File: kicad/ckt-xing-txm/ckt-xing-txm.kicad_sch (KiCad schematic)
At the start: 33 parts, among them J4 SM04B-SRSS, J5 SM04B-SRSS, U2 ATtiny861A-S, U3 AP7381-33Y

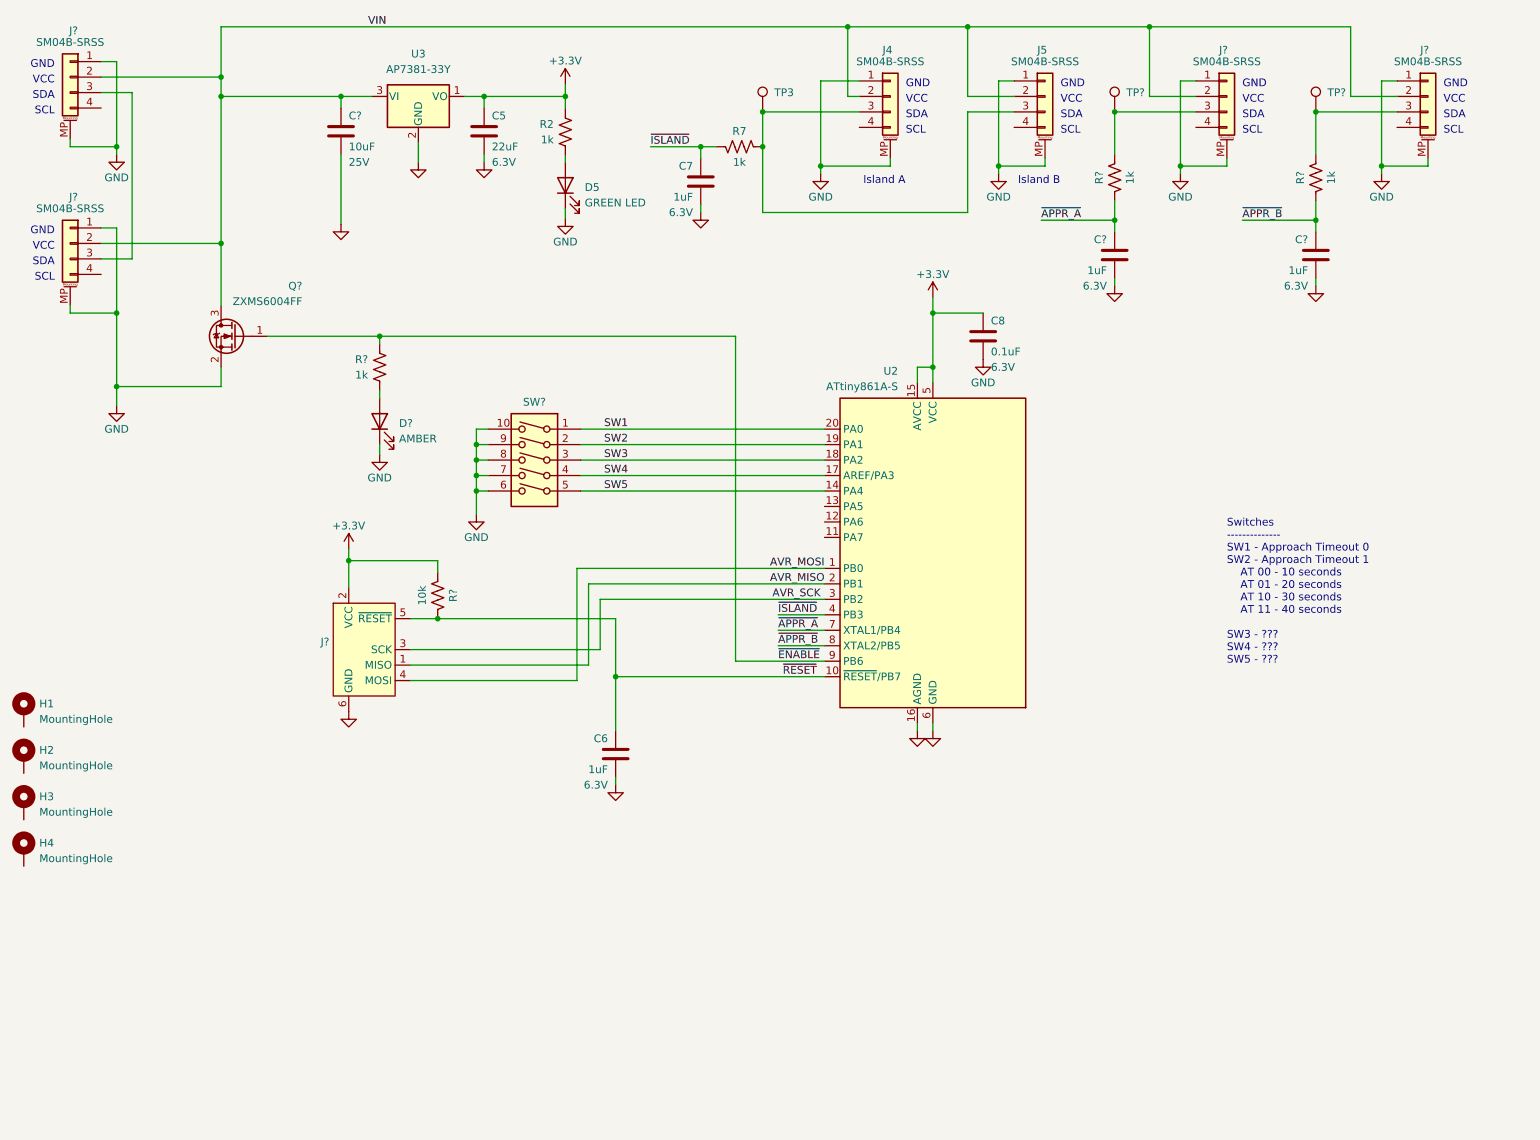
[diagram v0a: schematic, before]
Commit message: Add second track inputs to txm
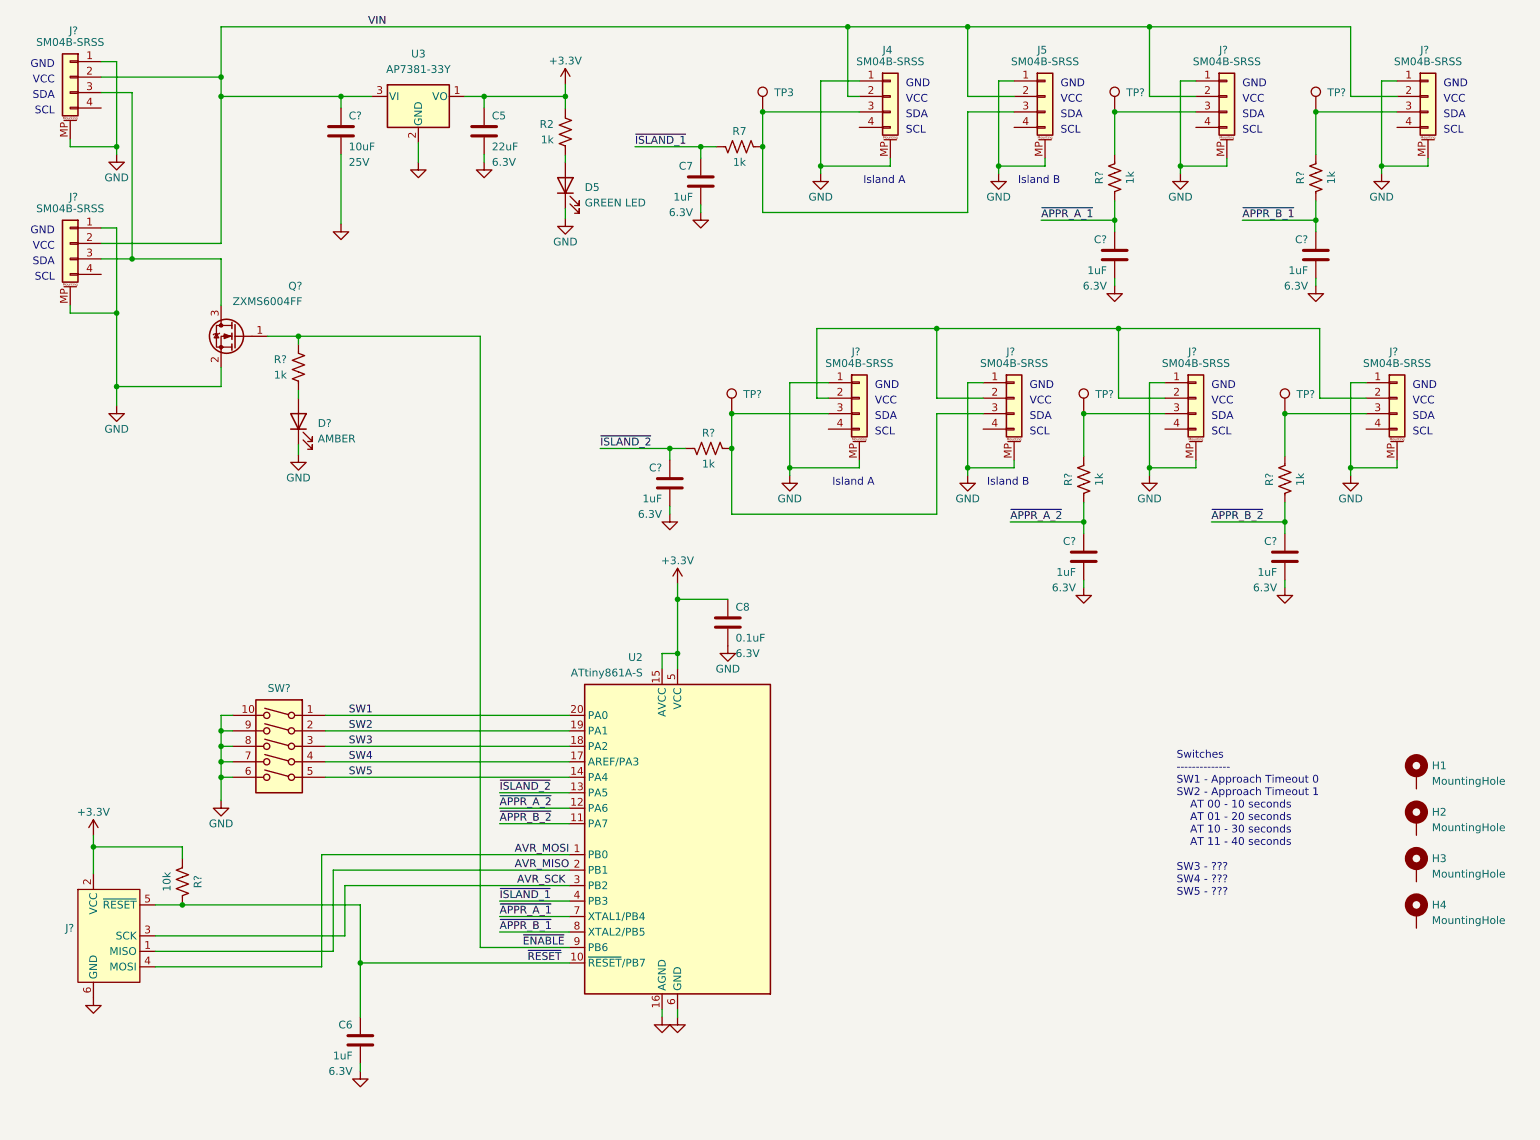
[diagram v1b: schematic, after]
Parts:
- added C? (x3): 1uF, Capacitor_SMD:C_0805_2012Metric, symbol Device:C
- added J? (x4): SM04B-SRSS, Connector_JST:JST_SH_SM04B-SRSS-TB_1x04-1MP_P1.00mm_Horizontal, symbol Connector_Generic_MountingPin:Conn_01x04_MountingPin
- added R? (x3): 1k, Resistor_SMD:R_0805_2012Metric, symbol Device:R_US
- added TP? (x3): TestPoint, TestPoint:TestPoint_Pad_D2.0mm, symbol Connector:TestPoint
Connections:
- net GND: now also C?.2, C?.2, C?.2, J?.1 (Pin_1), J?.1 (Pin_1), J?.1 (Pin_1), J?.1 (Pin_1), J?.MP (MountPin), J?.MP (MountPin), J?.MP (MountPin), J?.MP (MountPin)
- net VIN: no longer Q?.3 (D)
- net ~{APPR_B_2}: now reaches U2.11 (PA7)
- net ~{APPR_B_2}: now also C?.1, R?.2
- net ~{APPR_A_2}: now reaches U2.12 (PA6)
- net ~{APPR_A_2}: now also C?.1, R?.2
- net ~{ISLAND_2}: now reaches U2.13 (PA5)
- net ~{ISLAND_2}: now also C?.1, R?.2
- net at J?.3 (Pin_3), J?.3 (Pin_3): now also Q?.3 (D)
- net ~{APPR_A} renamed ~{APPR_A_1}
- net ~{APPR_B} renamed ~{APPR_B_1}
- net ~{ISLAND} renamed ~{ISLAND_1}
- new net: J?.3 (Pin_3), R?.1, TP?.1 (x2)
- new net: J?.2 (Pin_2), J?.2 (Pin_2), J?.2 (Pin_2), J?.2 (Pin_2)
- new net: J?.3 (Pin_3), J?.3 (Pin_3), R?.1, TP?.1
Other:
- moved on the sheet: C6, C8, D?, H1, H2, H3, H4, J?, R?, SW?, U2

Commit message: Initial layout of TXM board
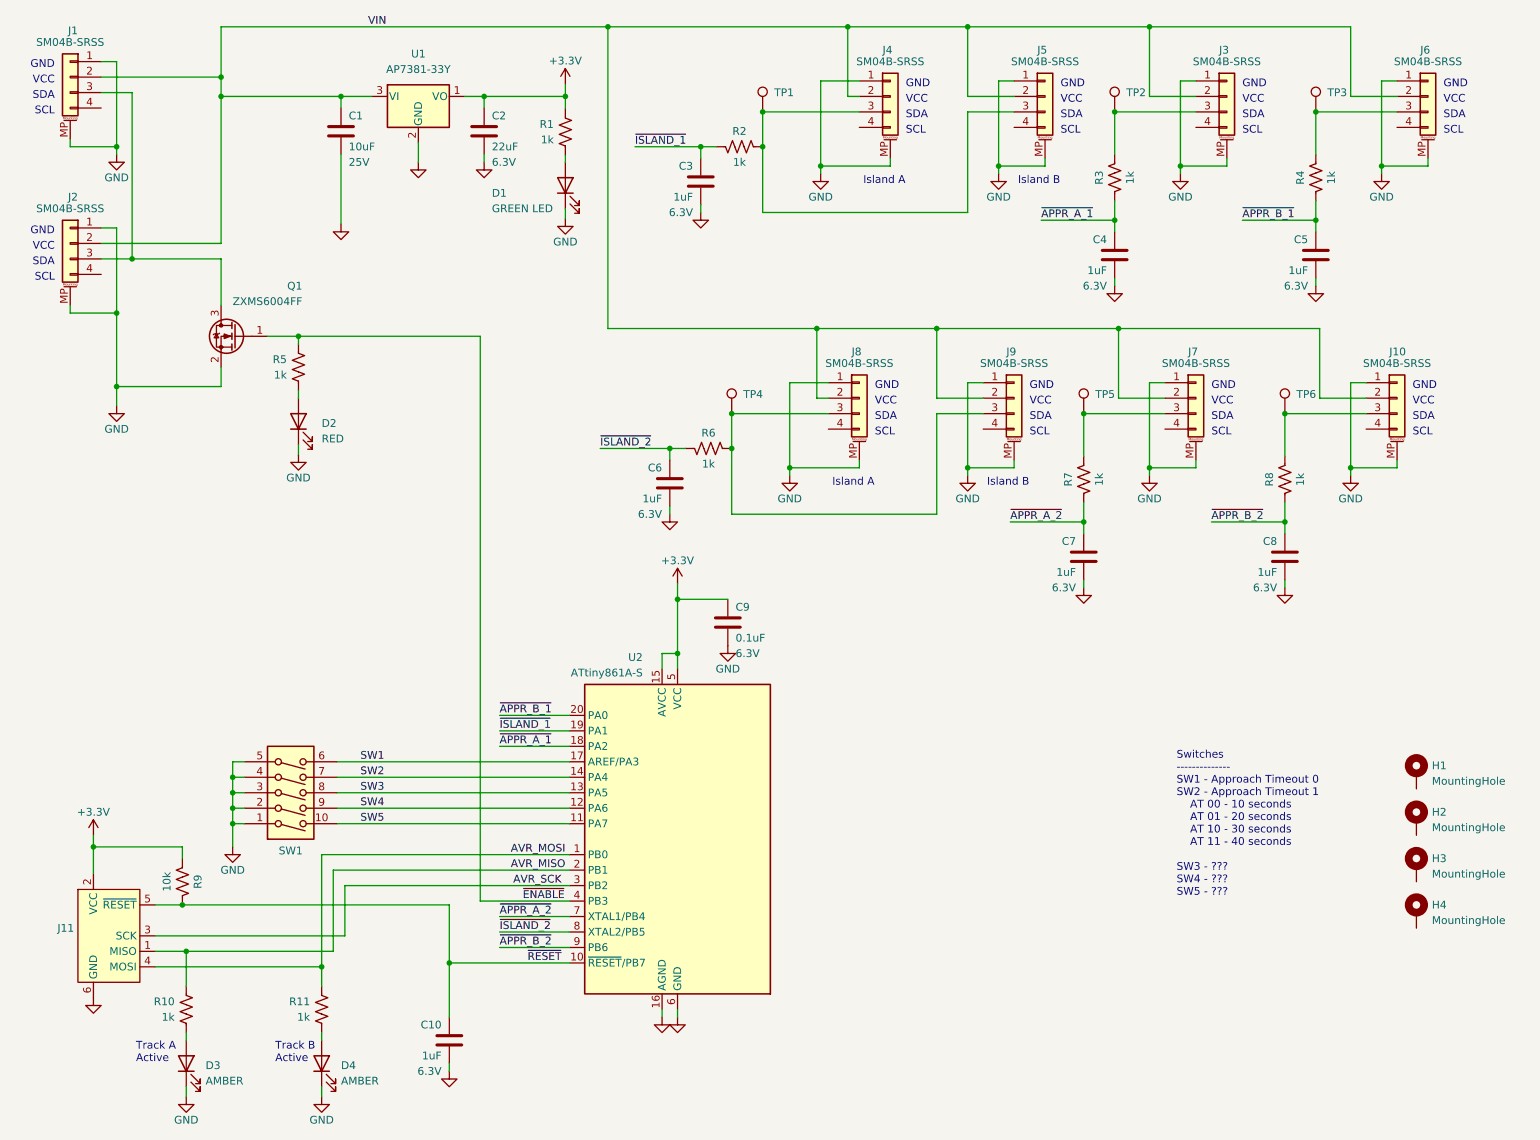
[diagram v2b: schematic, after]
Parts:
- removed SW?: SW_DIP_x05, ISE_UltraLibrarian:CST_219SMT, symbol Switch:SW_DIP_x05
- added D3, D4: AMBER, LED_SMD:LED_0805_2012Metric, symbol Device:LED
- added R10, R11: 1k, Resistor_SMD:R_0805_2012Metric, symbol Device:R_US
- added SW1: SW_DIP_x05, ISE_UltraLibrarian:CST_219SMT, symbol Switch:SW_DIP_x05
- D2: renamed from D?; value AMBER -> RED
- gave numbers to parts that had none: 28
- renumbered C6 to C10, C5 to C2, C7 to C3, C8 to C9, D5 to D1, R2 to R1, R7 to R2, TP3 to TP1, U3 to U1
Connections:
- net AVR_MISO: now also R10.2
- net AVR_MOSI: now also R11.2
- net GND: now also D3.1 (K), D4.1 (K), SW1.1, SW1.2, SW1.3, SW1.4, SW1.5
- net SW1: now also U2.17 (AREF/PA3), SW1.6; no longer U2.20 (PA0)
- net SW2: now also U2.14 (PA4), SW1.7; no longer U2.19 (PA1)
- net SW3: now also U2.13 (PA5), SW1.8; no longer U2.18 (PA2)
- net SW4: now also U2.12 (PA6), SW1.9; no longer U2.17 (AREF/PA3)
- net SW5: now also U2.11 (PA7), SW1.10; no longer U2.14 (PA4)
- net VIN: now also J10.2 (Pin_2), J7.2 (Pin_2), J8.2 (Pin_2), J9.2 (Pin_2)
- net ~{APPR_A_1}: now also U2.18 (PA2); no longer U2.7 (XTAL1/PB4)
- net ~{APPR_A_2}: now also U2.7 (XTAL1/PB4); no longer U2.12 (PA6)
- net ~{APPR_B_1}: now also U2.20 (PA0); no longer U2.8 (XTAL2/PB5)
- net ~{APPR_B_2}: now also U2.9 (PB6); no longer U2.11 (PA7)
- net ~{ENABLE}: now also U2.4 (PB3); no longer U2.9 (PB6)
- net ~{ISLAND_1}: now also U2.19 (PA1); no longer U2.4 (PB3)
- net ~{ISLAND_2}: now also U2.8 (XTAL2/PB5); no longer U2.13 (PA5)
- new net: D4.2 (A), R11.1
- new net: D3.2 (A), R10.1
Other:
- note added: "Track A Active"
- note added: "Track B Active"
- moved on the sheet: C10
